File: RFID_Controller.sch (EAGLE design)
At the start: 41 parts, among them IC2 MCP23017SP, K1 FTR-K1C, T1 BC547, T2 BC547

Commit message: -mod: more distance between drill and HV (upper left corner) -mod: TVS diode instead of Z-Diode -fix: additional resistor to SW Output pin to avoid short circuits. SW input pin measures now full voltage, not only Ube
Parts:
- removed C10, C9: 100p, rcl:C-EU050-024X044
- added C11, C12: 100n, rcl:C-EU050-025X075
- added R15: 1k, rcl:R-EU_0204/7
- D2: value 5.1V -> SM6T5A; device diode:ZENER-DIODEDO34-7 -> diode:SUPPRESSOR-SMBJ
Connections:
- removed net VCC: C9.1
- net 3V3: now also C12.1
- net 5V: now also C11.1; no longer C10.1
- net GND: now also C11.2, C12.2; no longer C10.2, C9.2
- net N$8: now also R15.1
- net SW: now also R15.2
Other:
- moved on the sheet: R5
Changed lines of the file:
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@@
 <part name="P+2" library="supply1" deviceset="VCC" device="" value="5V"/>
 <part name="P+3" library="supply1" deviceset="VCC" device="" value="5V"/>
-<part name="D2" library="diode" deviceset="ZENER-DIODE" device="DO34-7" value="5.1V"/>
 <part name="P+4" library="supply1" deviceset="VCC" device="" value="5V"/>
 <part name="GND7" library="supply1" deviceset="GND" device=""/>
@@
 <part name="R13" library="rcl" deviceset="R-EU_" device="0204/7" value="1k"/>
 <part name="R14" library="rcl" deviceset="R-EU_" device="0204/7" value="1k"/>
-<part name="C9" library="rcl" deviceset="C-EU" device="050-024X044" value="100p"/>
-<part name="C10" library="rcl" deviceset="C-EU" device="050-024X044" value="100p"/>
 <part name="P+16" library="supply1" deviceset="VCC" device="" value="5V"/>
 <part name="GND12" library="supply1" deviceset="GND" device=""/>
 <part name="P+17" library="supply1" deviceset="VCC" device="" value="3V3"/>
 <part name="GND13" library="supply1" deviceset="GND" device=""/>
+<part name="C11" library="rcl" deviceset="C-EU" device="050-025X075" value="100n"/>
+<part name="C12" library="rcl" deviceset="C-EU" device="050-025X075" value="100n"/>
+<part name="R15" library="rcl" deviceset="R-EU_" device="0204/7" value="1k"/>
+<part name="D2" library="diode" deviceset="SUPPRESSOR-" device="SMBJ" value="SM6T5A"/>
 </parts>
 <sheets>
@@
 <instance part="D1" gate="G$1" x="326.39" y="135.89" rot="R90"/>
 <instance part="GND6" gate="1" x="336.55" y="110.49"/>
-<instance part="R5" gate="G$1" x="170.18" y="73.66" rot="R180"/>
+<instance part="R5" gate="G$1" x="182.88" y="73.66" rot="R180"/>
 <instance part="P+2" gate="VCC" x="336.55" y="151.13"/>
 <instance part="P+3" gate="VCC" x="173.99" y="124.46" smashed="yes" rot="R270">
 <attribute name="VALUE" x="173.99" y="121.92" size="1.778" layer="96" rot="R180"/>
 </instance>
-<instance part="D2" gate="G$1" x="55.88" y="236.22" rot="R90"/>
 <instance part="P+4" gate="VCC" x="55.88" y="246.38"/>
 <instance part="GND7" gate="1" x="55.88" y="223.52"/>
@@
 <instance part="R13" gate="G$1" x="121.92" y="86.36" rot="R270"/>
 <instance part="R14" gate="G$1" x="129.54" y="86.36" rot="R270"/>
-<instance part="C9" gate="G$1" x="264.16" y="134.62"/>
-<instance part="C10" gate="G$1" x="99.06" y="132.08"/>
 <instance part="P+16" gate="VCC" x="99.06" y="143.51" smashed="yes">
 <attribute name="VALUE" x="101.6" y="143.51" size="1.778" layer="96" rot="R270"/>
@@
 </instance>
 <instance part="GND13" gate="1" x="264.16" y="120.65"/>
+<instance part="C11" gate="G$1" x="99.06" y="132.08"/>
+<instance part="C12" gate="G$1" x="264.16" y="134.62"/>
+<instance part="R15" gate="G$1" x="167.64" y="71.12" rot="R180"/>
+<instance part="D2" gate="G$1" x="55.88" y="236.22"/>
 </instances>
 <busses>
@@
 <pinref part="C2" gate="G$1" pin="2"/>
 <wire x1="43.18" y1="228.6" x2="43.18" y2="231.14" width="0.1524" layer="91"/>
-<pinref part="D2" gate="G$1" pin="A"/>
-<wire x1="55.88" y1="233.68" x2="55.88" y2="228.6" width="0.1524" layer="91"/>
 <wire x1="55.88" y1="228.6" x2="43.18" y2="228.6" width="0.1524" layer="91"/>
 <pinref part="GND7" gate="1" pin="GND"/>
 <wire x1="55.88" y1="226.06" x2="55.88" y2="228.6" width="0.1524" layer="91"/>
-<junction x="55.88" y="228.6"/>
 <pinref part="C1" gate="G$1" pin="-"/>
 <wire x1="35.56" y1="231.14" x2="35.56" y2="228.6" width="0.1524" layer="91"/>
@@
 <wire x1="35.56" y1="228.6" x2="27.94" y2="228.6" width="0.1524" layer="91"/>
 <junction x="35.56" y="228.6"/>
+<wire x1="55.88" y1="233.68" x2="55.88" y2="228.6" width="0.1524" layer="91"/>
+<junction x="55.88" y="228.6"/>
+<pinref part="D2" gate="G$1" pin="A"/>
 </segment>
 <segment>
@@
 </segment>
 <segment>
-<pinref part="C10" gate="G$1" pin="2"/>
-<wire x1="99.06" y1="127" x2="99.06" y2="121.92" width="0.1524" layer="91"/>
-<pinref part="GND12" gate="1" pin="GND"/>
-</segment>
-<segment>
-<pinref part="C9" gate="G$1" pin="2"/>
 <pinref part="GND13" gate="1" pin="GND"/>
 <wire x1="264.16" y1="129.54" x2="264.16" y2="123.19" width="0.1524" layer="91"/>
+<pinref part="C12" gate="G$1" pin="2"/>
+</segment>
+<segment>
+<pinref part="GND12" gate="1" pin="GND"/>
+<pinref part="C11" gate="G$1" pin="2"/>
+<wire x1="99.06" y1="121.92" x2="99.06" y2="127" width="0.1524" layer="91"/>
 </segment>
 </net>
@@
 </segment>
 <segment>
-<pinref part="D2" gate="G$1" pin="C"/>
-<wire x1="55.88" y1="241.3" x2="55.88" y2="238.76" width="0.1524" layer="91"/>
 <pinref part="P+4" gate="VCC" pin="VCC"/>
 <wire x1="55.88" y1="241.3" x2="55.88" y2="243.84" width="0.1524" layer="91"/>
@@
 <wire x1="55.88" y1="241.3" x2="43.18" y2="241.3" width="0.1524" layer="91"/>
 <junction x="43.18" y="241.3"/>
+<wire x1="55.88" y1="241.3" x2="55.88" y2="238.76" width="0.1524" layer="91"/>
+<pinref part="D2" gate="G$1" pin="C"/>
 </segment>
 <segment>
@@
 </segment>
 <segment>
-<pinref part="C10" gate="G$1" pin="1"/>
-<wire x1="99.06" y1="142.24" x2="99.06" y2="134.62" width="0.1524" layer="91"/>
+<pinref part="C11" gate="G$1" pin="1"/>
+<pinref part="P+16" gate="VCC" pin="VCC"/>
+<wire x1="99.06" y1="134.62" x2="99.06" y2="140.97" width="0.1524" layer="91"/>
 </segment>
 </net>
@@
 <wire x1="130.81" y1="251.46" x2="130.81" y2="248.92" width="0.1524" layer="91"/>
 </segment>
+<segment>
+<pinref part="P+17" gate="VCC" pin="VCC"/>
+<wire x1="264.16" y1="137.16" x2="264.16" y2="144.78" width="0.1524" layer="91"/>
+<pinref part="C12" gate="G$1" pin="1"/>
+</segment>
 </net>
 <net name="MISO" class="0">
@@
 <segment>
 <pinref part="IC2" gate="G$1" pin="GPB1"/>
-<label x="182.88" y="73.66" size="1.778" layer="95"/>
+<wire x1="160.02" y1="71.12" x2="162.56" y2="71.12" width="0.1524" layer="91"/>
+<pinref part="R15" gate="G$1" pin="2"/>
+</segment>
+<segment>
 <pinref part="R5" gate="G$1" pin="1"/>
-<wire x1="175.26" y1="73.66" x2="180.34" y2="73.66" width="0.1524" layer="91"/>
-<wire x1="160.02" y1="71.12" x2="180.34" y2="71.12" width="0.1524" layer="91"/>
-<wire x1="180.34" y1="71.12" x2="180.34" y2="73.66" width="0.1524" layer="91"/>
-<wire x1="180.34" y1="73.66" x2="182.88" y2="73.66" width="0.1524" layer="91"/>
-<junction x="180.34" y="73.66"/>
+<wire x1="187.96" y1="73.66" x2="193.04" y2="73.66" width="0.1524" layer="91"/>
+<label x="193.04" y="73.66" size="1.778" layer="95"/>
 </segment>
 </net>
@@
 <pinref part="R5" gate="G$1" pin="2"/>
 <pinref part="IC2" gate="G$1" pin="GPB0"/>
-<wire x1="165.1" y1="73.66" x2="160.02" y2="73.66" width="0.1524" layer="91"/>
-</segment>
-</net>
-<net name="VCC" class="0">
-<segment>
-<pinref part="C9" gate="G$1" pin="1"/>
-<pinref part="P+17" gate="VCC" pin="VCC"/>
-<wire x1="264.16" y1="137.16" x2="264.16" y2="144.78" width="0.1524" layer="91"/>
-</segment>
-</net>
+<wire x1="177.8" y1="73.66" x2="175.26" y2="73.66" width="0.1524" layer="91"/>
+<pinref part="R15" gate="G$1" pin="1"/>
+<wire x1="175.26" y1="73.66" x2="160.02" y2="73.66" width="0.1524" layer="91"/>
+<wire x1="172.72" y1="71.12" x2="175.26" y2="71.12" width="0.1524" layer="91"/>
+<wire x1="175.26" y1="71.12" x2="175.26" y2="73.66" width="0.1524" layer="91"/>
+<junction x="175.26" y="73.66"/>
+</segment>
+</net>

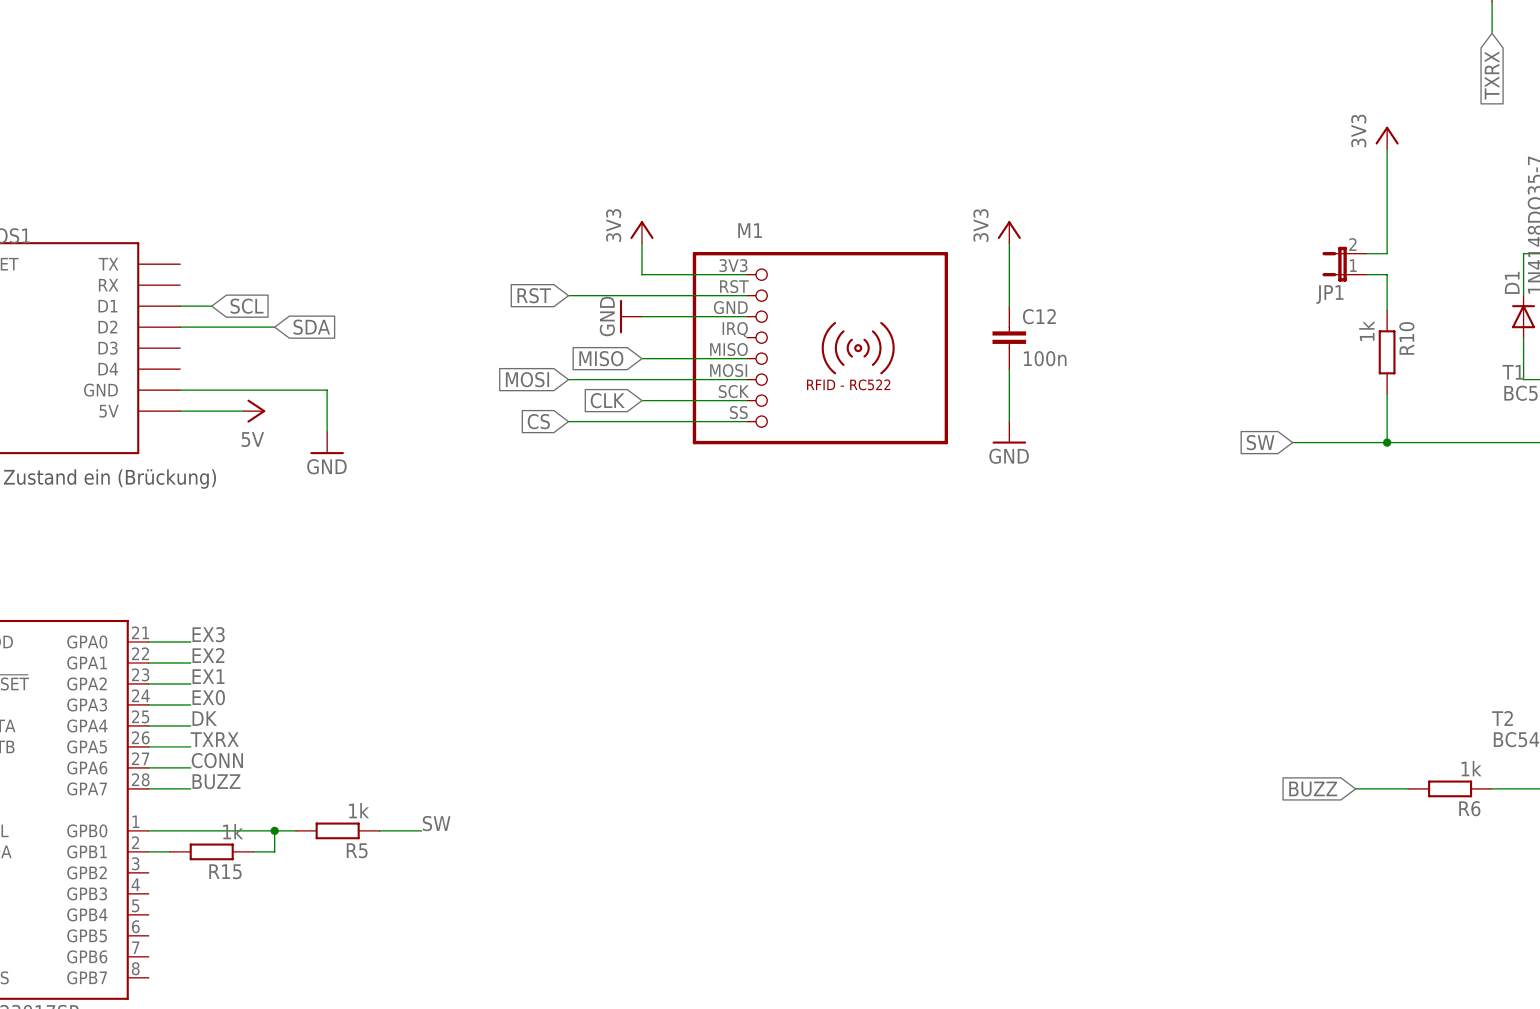
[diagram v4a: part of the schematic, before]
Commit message: -mod: Board layout and Schematic in ELAB optimized
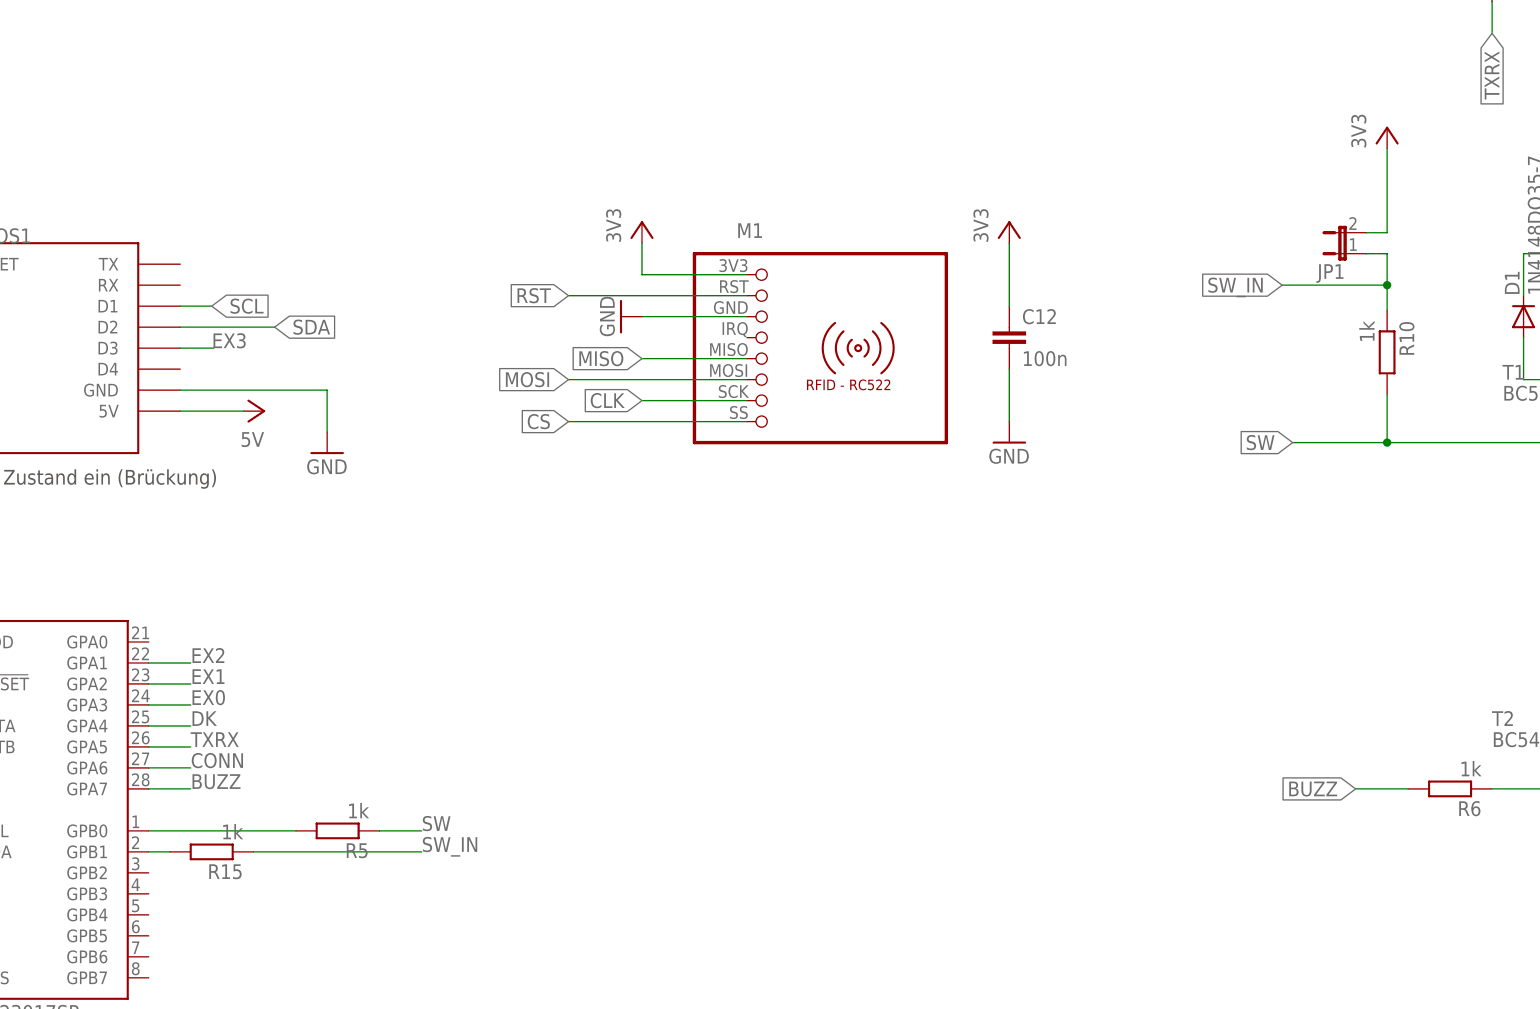
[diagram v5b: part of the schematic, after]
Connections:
- removed net N$12: JP1.1, R10.1
- new net SW_IN: JP1.1, R10.1, R15.1
- net EX3: now also WEMOS1.D3; no longer IC2.GPA0
- net N$8: no longer R15.1
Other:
- moved on the sheet: JP1
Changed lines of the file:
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@@
 </instance>
 <instance part="GND9" gate="1" x="217.17" y="135.89" rot="R270"/>
-<instance part="JP1" gate="A" x="304.8" y="140.97" rot="R90"/>
+<instance part="JP1" gate="A" x="304.8" y="143.51" rot="R90"/>
 <instance part="P+6" gate="VCC" x="309.88" y="158.75" smashed="yes">
 <attribute name="VALUE" x="307.34" y="156.21" size="1.778" layer="96" rot="R90"/>
@@
 <segment>
 <pinref part="JP1" gate="A" pin="2"/>
-<wire x1="307.34" y1="143.51" x2="309.88" y2="143.51" width="0.1524" layer="91"/>
-<wire x1="309.88" y1="143.51" x2="309.88" y2="156.21" width="0.1524" layer="91"/>
+<wire x1="307.34" y1="146.05" x2="309.88" y2="146.05" width="0.1524" layer="91"/>
+<wire x1="309.88" y1="146.05" x2="309.88" y2="156.21" width="0.1524" layer="91"/>
 <pinref part="P+6" gate="VCC" pin="VCC"/>
 </segment>
@@
 </segment>
 </net>
-<net name="N$12" class="0">
-<segment>
-<pinref part="JP1" gate="A" pin="1"/>
-<wire x1="307.34" y1="140.97" x2="309.88" y2="140.97" width="0.1524" layer="91"/>
-<pinref part="R10" gate="G$1" pin="1"/>
-<wire x1="309.88" y1="140.97" x2="309.88" y2="136.652" width="0.1524" layer="91"/>
-</segment>
-</net>
 <net name="N$2" class="0">
 <segment>
@@
 </segment>
 <segment>
-<pinref part="IC2" gate="G$1" pin="GPA0"/>
-<wire x1="160.02" y1="96.52" x2="165.1" y2="96.52" width="0.1524" layer="91"/>
-<label x="165.1" y="96.52" size="1.778" layer="95"/>
-</segment>
-<segment>
 <label x="271.78" y="213.36" size="1.778" layer="95"/>
 <wire x1="271.78" y1="213.36" x2="281.94" y2="213.36" width="0.1524" layer="91"/>
 <pinref part="JP5" gate="A" pin="9"/>
 </segment>
+<segment>
+<pinref part="WEMOS1" gate="D1" pin="D3"/>
+<wire x1="163.83" y1="132.08" x2="167.894" y2="132.08" width="0.1524" layer="91"/>
+<label x="167.64" y="132.08" size="1.778" layer="95"/>
+</segment>
 </net>
 <net name="N$8" class="0">
@@
 <pinref part="R5" gate="G$1" pin="2"/>
 <pinref part="IC2" gate="G$1" pin="GPB0"/>
-<wire x1="177.8" y1="73.66" x2="175.26" y2="73.66" width="0.1524" layer="91"/>
+<wire x1="177.8" y1="73.66" x2="160.02" y2="73.66" width="0.1524" layer="91"/>
+</segment>
+</net>
+<net name="SW_IN" class="0">
+<segment>
 <pinref part="R15" gate="G$1" pin="1"/>
-<wire x1="175.26" y1="73.66" x2="160.02" y2="73.66" width="0.1524" layer="91"/>
-<wire x1="172.72" y1="71.12" x2="175.26" y2="71.12" width="0.1524" layer="91"/>
-<wire x1="175.26" y1="71.12" x2="175.26" y2="73.66" width="0.1524" layer="91"/>
-<junction x="175.26" y="73.66"/>
-</segment>
-</net>
+<wire x1="172.72" y1="71.12" x2="193.04" y2="71.12" width="0.1524" layer="91"/>
+<label x="193.04" y="71.12" size="1.778" layer="95"/>
+</segment>
+<segment>
+<pinref part="JP1" gate="A" pin="1"/>
+<wire x1="307.34" y1="143.51" x2="309.88" y2="143.51" width="0.1524" layer="91"/>
+<pinref part="R10" gate="G$1" pin="1"/>
+<wire x1="309.88" y1="143.51" x2="309.88" y2="139.7" width="0.1524" layer="91"/>
+<wire x1="309.88" y1="139.7" x2="309.88" y2="136.652" width="0.1524" layer="91"/>
+<wire x1="309.88" y1="139.7" x2="297.18" y2="139.7" width="0.1524" layer="91"/>
+<junction x="309.88" y="139.7"/>
+<label x="297.18" y="139.7" size="1.778" layer="95" rot="R180" xref="yes"/>
+</segment>
+</net>
